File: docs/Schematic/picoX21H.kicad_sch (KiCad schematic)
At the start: 8 parts, among them J1 MIDI in, J2 Debug, J4 Debug, SW1 RST, U1 Pico 2 (RP2350), U3 H11L1

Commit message: More work on schematic
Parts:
- added J3: Stereo phones out, Connector_Audio:Jack_3.5mm_CUI_SJ1-3523N_Horizontal, symbol Connector_Audio:AudioJack2_Ground
- added J5: Stereo line out, Connector_Audio:Jack_3.5mm_CUI_SJ1-3523N_Horizontal, symbol Connector_Audio:AudioJack2_Ground
- added R2, R3, R4, R5, R6, R7, R8, R9: 120, symbol Device:R
- added U2: Pico-Audio, RPi_Pico:RPi_Pico_SMD_TH, symbol MCU_RaspberryPi_and_Boards:Pimoroni Pico-Audio
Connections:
- net +5V: now also U2.39 (VSYS)
- net Earth: now also U2.13 (GND), U2.18 (GND), U2.23 (GND), U2.28 (GND), U2.3 (GND), U2.33 (GND), U2.38 (GND), U2.8 (GND)
- net MIDI 31250 baud 8-N-1: now also U1.29 (GPIO22); no longer U1.27 (GPIO21)
- net at D1.2 (A), J1.5, U3.2: now also J1.4, R1.2
- net at U1.11 (GPIO8): now also R9.1
- net at U1.12 (GPIO9): now also R8.1
- net at U1.14 (GPIO10): now also R7.1
- net at U1.15 (GPIO11): now also R6.1
- net at U1.16 (GPIO12): now also R5.1
- net at U1.17 (GPIO13): now also R4.1
- net at U1.19 (GPIO14): now also R3.1
- net at U1.20 (GPIO15): now also R2.1
- net I2S SD: now reaches U1.25 (GPIO19)
- net I2S SD: now also U2.12 (DIN)
- net I2S LR 49.096 KHz: now reaches U1.26 (GPIO20)
- net I2S LR 49.096 KHz: now also U2.15 (LRCLK)
- new net: J5.G, U2. (PHONES_OUT_R)
- new net: J5.S, U2. (PHONES_OUT_R)
- new net: J5.T, U2. (PHONES_OUT_R)
- new net: J3.G, U2. (PHONES_OUT_R)
- new net: J3.S, U2. (PHONES_OUT_R)
- new net: J3.T, U2. (PHONES_OUT_R)
- new net I2S CLK 1.571072 MHz: U1.27 (GPIO21), U2.14 (SCLK)
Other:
- note added: "OPTIONAL Physical MIDI In"
- note added: "PIMORONI Pico Audio I2S DAC"
- note removed: "OPTIONAL I/O"
- moved on the sheet: D1, J1, R1, SW1, U3

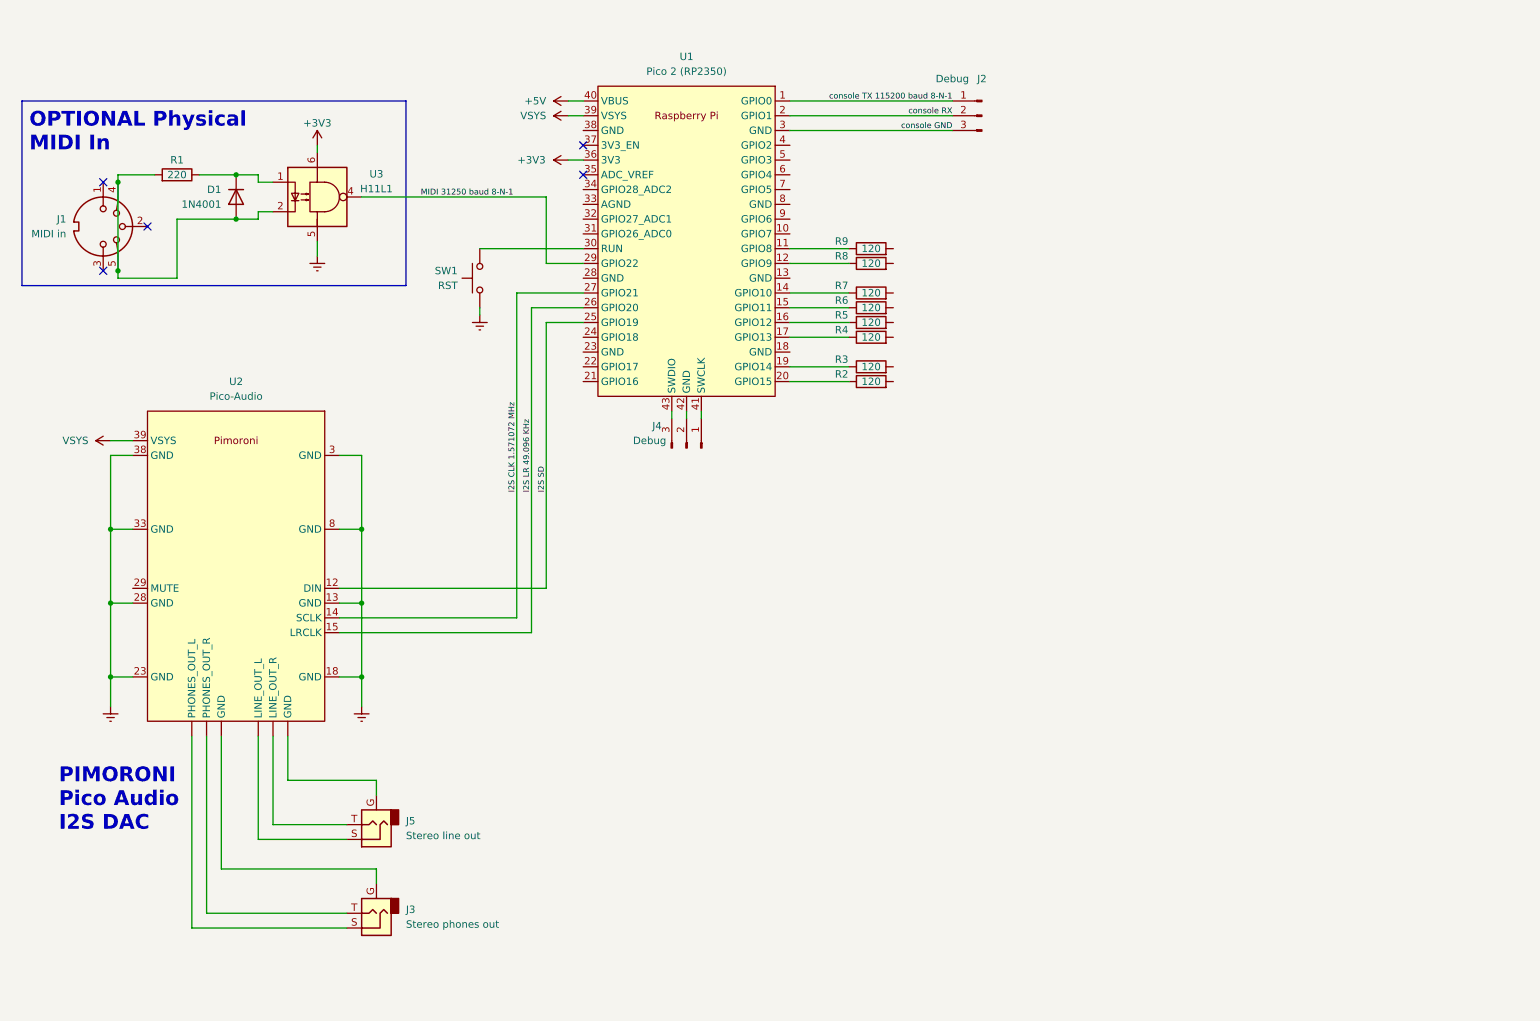
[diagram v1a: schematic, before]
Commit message: Re-work pin assignments for easier layout
+ also improved documentation
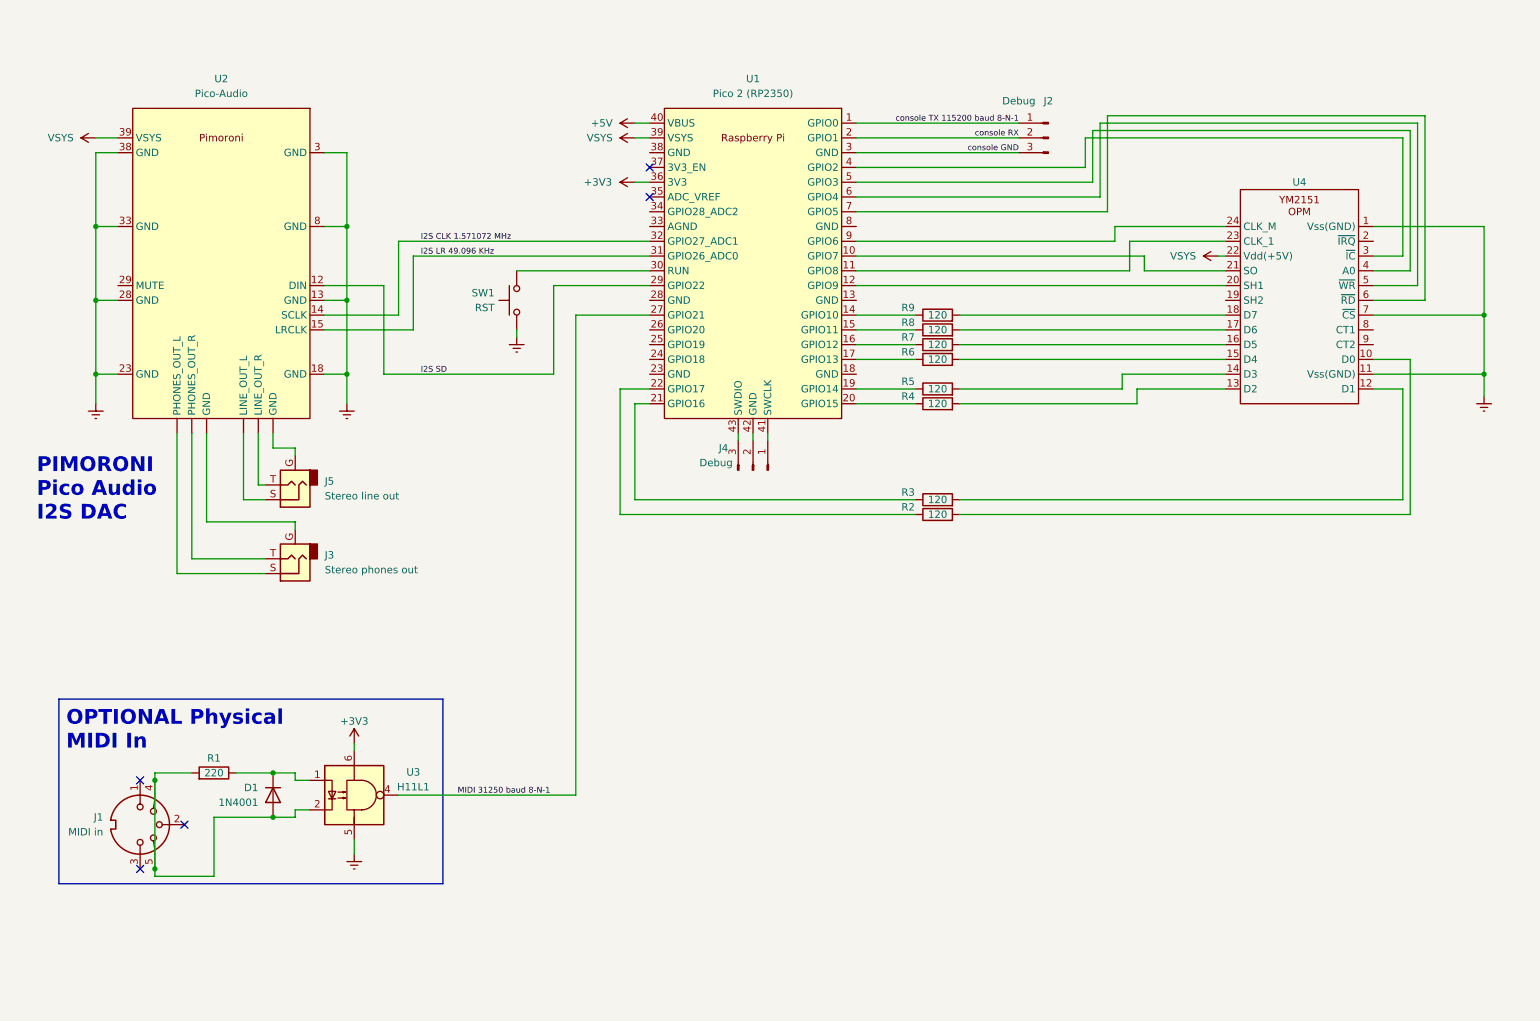
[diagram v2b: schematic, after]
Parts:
- added U4: ~, symbol MCU_RaspberryPi_and_Boards:YM2151
- U1: footprint Package_DIP:DIP-40_W25.4mm_Socket -> RPi_Pico:RPi_Pico_SMD_TH
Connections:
- net +5V: now also U4.22 (Vdd(+5V))
- net Earth: now also U4.1 (Vss(GND)), U4.11 (Vss(GND)), U4.7 (~{CS})
- net I2S CLK 1.571072 MHz: now also U1.32 (GPIO27_ADC1); no longer U1.27 (GPIO21)
- net I2S LR 49.096 KHz: now also U1.31 (GPIO26_ADC0); no longer U1.26 (GPIO20)
- net I2S SD: now also U1.29 (GPIO22); no longer U1.25 (GPIO19)
- net MIDI 31250 baud 8-N-1: now also U1.27 (GPIO21); no longer U1.29 (GPIO22)
- net at U1.10 (GPIO7): now also U4.21 (SO)
- net at U1.11 (GPIO8): now also U4.23 (CLK_1); no longer R9.1
- net at U1.12 (GPIO9): now also U4.20 (SH1); no longer R8.1
- net at U1.14 (GPIO10): now also R9.1; no longer R7.1
- net at U1.15 (GPIO11): now also R8.1; no longer R6.1
- net at U1.16 (GPIO12): now also R7.1; no longer R5.1
- net at U1.17 (GPIO13): now also R6.1; no longer R4.1
- net at U1.19 (GPIO14): now also R5.1; no longer R3.1
- net at U1.20 (GPIO15): now also R4.1; no longer R2.1
- net at U1.21 (GPIO16): now also R3.1
- net at U1.22 (GPIO17): now also R2.1
- net at U1.4 (GPIO2): now also U4.3 (~{IC})
- net at U1.5 (GPIO3): now also U4.4 (A0)
- net at U1.6 (GPIO4): now also U4.5 (~{WR})
- net at U1.7 (GPIO5): now also U4.6 (~{RD})
- net at U1.9 (GPIO6): now also U4.24 (CLK_M)
- net at R8.2: now also U4.17 (D6)
- net at R6.2: now also U4.15 (D4)
- net at R3.2: now also U4.12 (D1)
- net at R9.2: now also U4.18 (D7)
- net at R2.2: now also U4.10 (D0)
- net at R7.2: now also U4.16 (D5)
- net at R4.2: now also U4.13 (D2)
- net at R5.2: now also U4.14 (D3)
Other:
- moved on the sheet: D1, J1, J2, J3, J4, J5, R1, R2, R3, R4, R5, R6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

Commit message: Further pin assignment changes
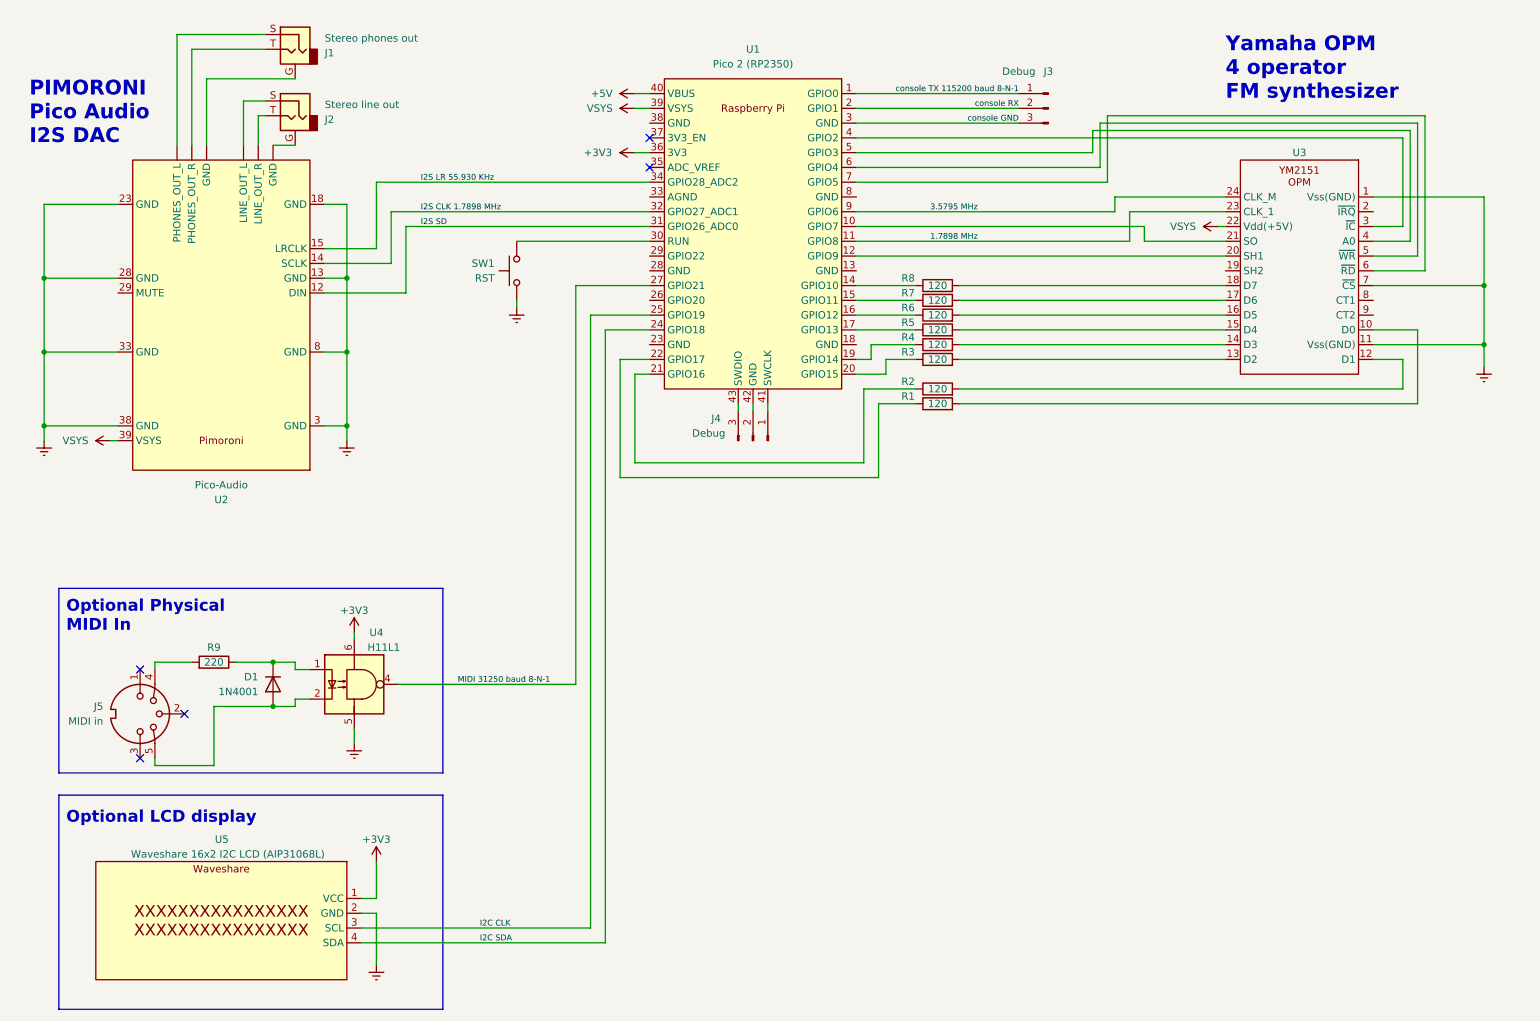
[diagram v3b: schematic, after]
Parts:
- added U5: Waveshare 16x2 I2C LCD (AIP31068L), RPi_Pico:RPi_Pico_SMD_TH, symbol MCU_RaspberryPi_and_Boards:Waveshare 16x2 I2C LCD
- renumbered J3 to J1, J5 to J2, J2 to J3, J1 to J5, R2 to R1, R3 to R2, R4 to R3, R5 to R4, R6 to R5, R7 to R6, R8 to R7, R9 to R8, R1 to R9, U4 to U3, U3 to U4
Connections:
- net +3V3: now also U5.1 (VCC)
- net Earth: now also U5.2 (GND)
- net I2S SD: now also U1.31 (GPIO26_ADC0); no longer U1.29 (GPIO22)
- net at D1.2 (A), J5.5, U4.2: no longer J5.4, R9.2
- net 1.7898 MHz: now reaches U1.11 (GPIO8), U3.23 (CLK_1)
- net I2C SDA: now reaches U1.24 (GPIO18)
- net I2C SDA: now also U5.4 (SDA)
- net I2C CLK: now reaches U1.25 (GPIO19)
- net I2C CLK: now also U5.3 (SCL)
- net I2S LR 55.930 KHz: now reaches U1.34 (GPIO28_ADC2)
- net I2S LR 55.930 KHz: now also U2.15 (LRCLK)
- net 3.5795 MHz: now reaches U1.9 (GPIO6), U3.24 (CLK_M)
- net I2S CLK 1.571072 MHz renamed I2S CLK 1.7898 MHz
- removed net I2S LR 49.096 KHz: U1.31 (GPIO26_ADC0), U2.15 (LRCLK)
- new net: J5.4, R9.2
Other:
- note added: "Optional LCD display"
- note added: "Optional Physical MIDI In"
- note added: "Yamaha OPM 4 operator FM synthesizer"
- note removed: "OPTIONAL Physical MIDI In"
- moved on the sheet: D1, J1, J2, J3, J4, J5, R1, R2, R3, R4, R5, R6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

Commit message: Mirror schematic to give a birds eye view
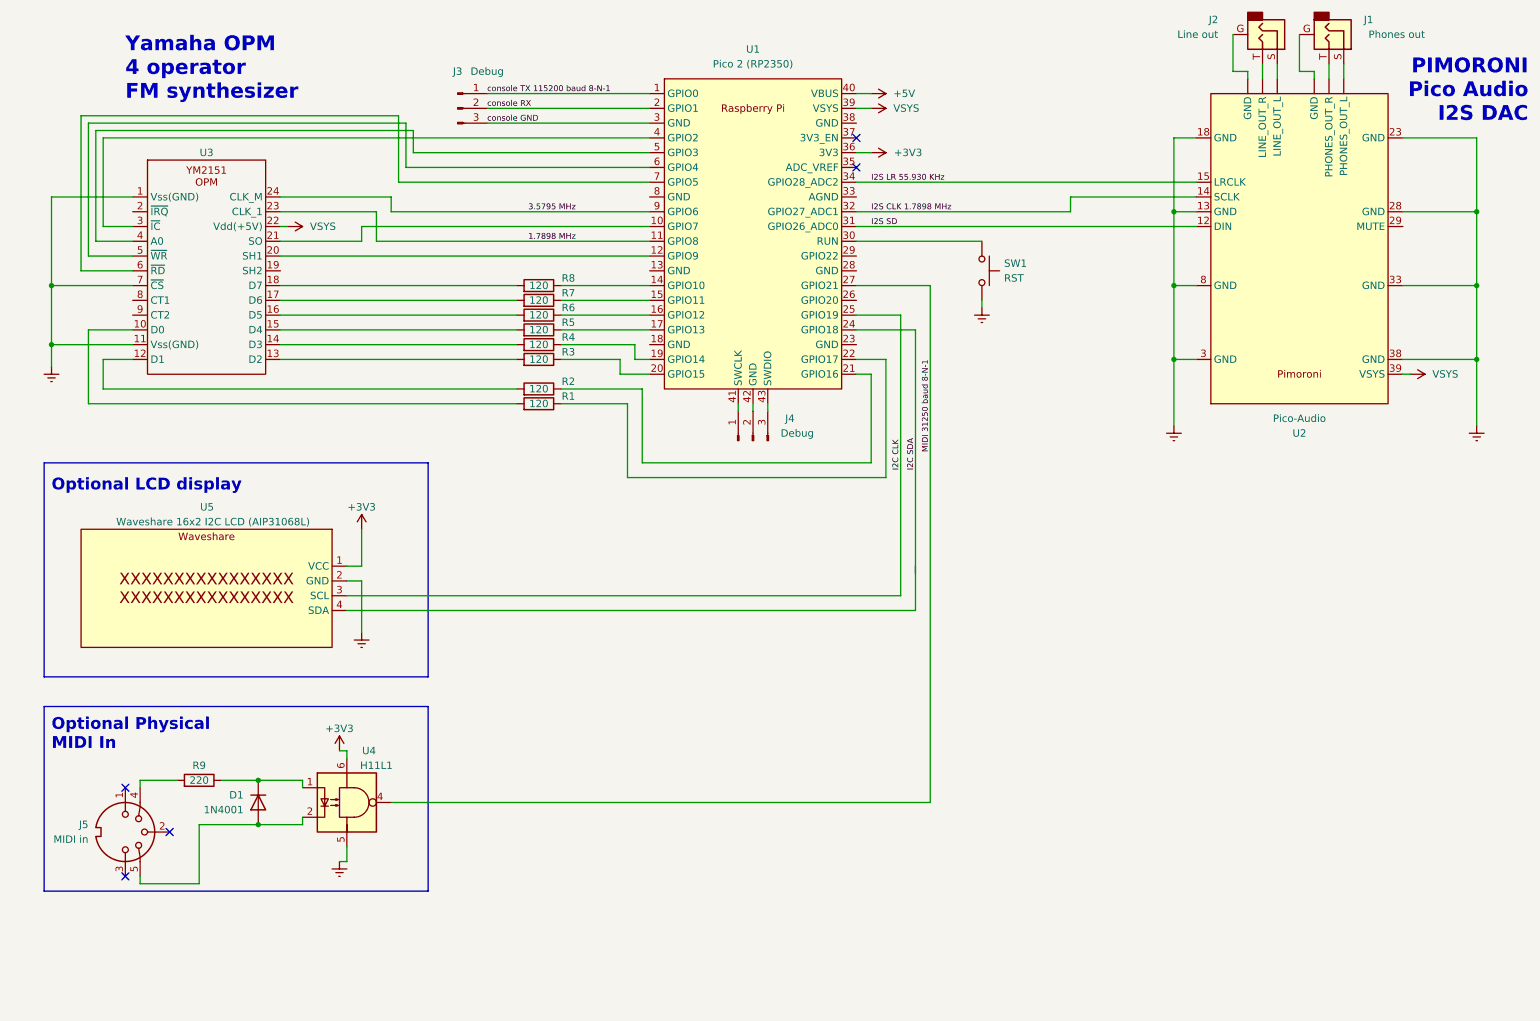
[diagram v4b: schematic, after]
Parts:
- J1: value Stereo phones out -> Phones out
- J2: value Stereo line out -> Line out
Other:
- moved on the sheet: D1, J1, J2, J3, J4, J5, R1, R2, R3, R4, R5, R6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
